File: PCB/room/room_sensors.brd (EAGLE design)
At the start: 90 x 90 mm, 112 parts, among them CON1 95278-101A14LF, CON2 95278-101A14LF, CON3 OV2640-HDF3M-811FRONTLOOKING, U1 BH1750FVI-TR, U12 LMR16020, U14 WM8974, U17 RT9043GB, U18 RT9043GB, U2 BME280, U3 CCS811B-JOPD500, U4 SN65HVD11DR, U5 SN65HVD11DR, U6 SN65HVD11DR, U7 SN65HVD11DR, U8 MAX14830ETMT, Y1 X1G004171001800 12MHz

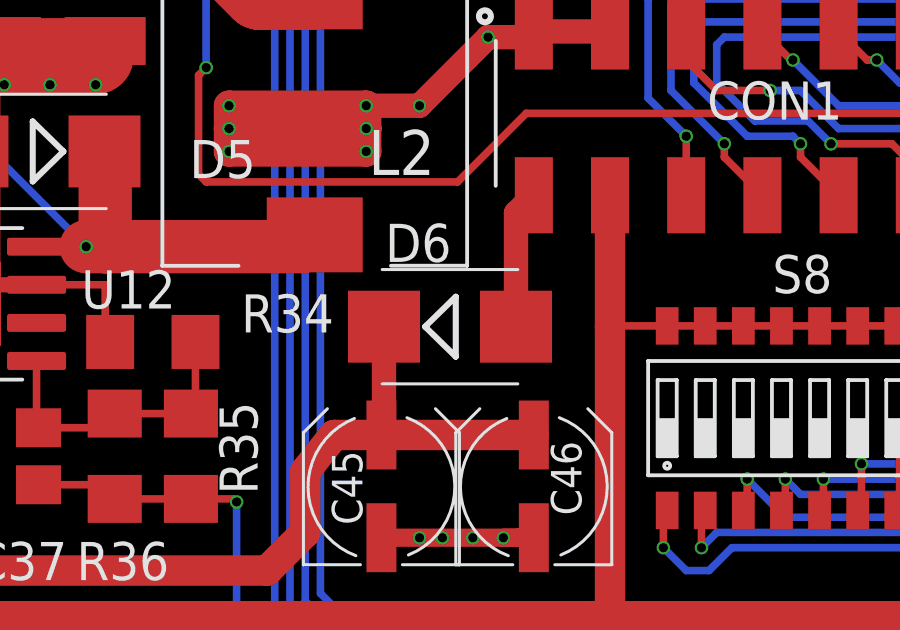
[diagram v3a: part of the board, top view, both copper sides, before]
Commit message: finished interface PCB
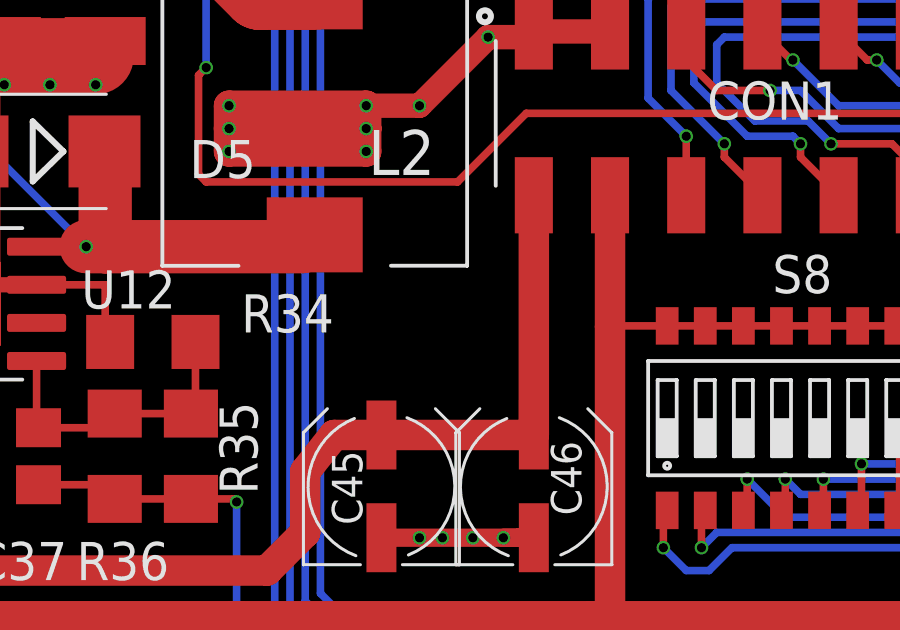
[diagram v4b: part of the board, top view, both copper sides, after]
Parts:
- removed D6: B360B-13-F, diode:SMB
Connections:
- removed net N$31: CON1.2, D6.A
- net +24V: now also CON1.2; no longer D6.C
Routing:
- net N$31: track 4.63 -> 0.00 mm
- net +24V: track 49.2 -> 53.6 mm
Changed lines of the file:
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@@
 <grid distance="10" unitdist="mil" unit="mil" style="lines" multiple="1" display="no" altdistance="1" altunitdist="mil" altunit="mil"/>
 <layers>
-<layer number="1" name="Top" color="4" fill="1" visible="no" active="yes"/>
+<layer number="1" name="Top" color="4" fill="1" visible="yes" active="yes"/>
 <layer number="2" name="Route2" color="1" fill="3" visible="no" active="no"/>
 <layer number="3" name="Route3" color="4" fill="3" visible="no" active="no"/>
@@
 <layer number="14" name="Route14" color="1" fill="6" visible="no" active="no"/>
 <layer number="15" name="Route15" color="4" fill="6" visible="no" active="no"/>
-<layer number="16" name="Bottom" color="1" fill="1" visible="yes" active="yes"/>
+<layer number="16" name="Bottom" color="1" fill="1" visible="no" active="yes"/>
 <layer number="17" name="Pads" color="2" fill="1" visible="no" active="yes"/>
 <layer number="18" name="Vias" color="2" fill="1" visible="no" active="yes"/>
-<layer number="19" name="Unrouted" color="6" fill="1" visible="no" active="yes"/>
+<layer number="19" name="Unrouted" color="6" fill="1" visible="yes" active="yes"/>
 <layer number="20" name="Dimension" color="15" fill="1" visible="no" active="yes"/>
 <layer number="21" name="tPlace" color="7" fill="1" visible="no" active="yes"/>
@@
 <attribute name="NAME" x="69.68003125" y="25.76643125" size="2.08761875" layer="25" ratio="10" rot="SR270"/>
 </element>
-<element name="D6" library="diode" package="SMB" value="B360B-13-F" x="35.306" y="17.018"/>
 </elements>
 <signals>
@@
 <wire x1="13.6525" y1="11.7475" x2="13.6525" y2="18.285" width="1.016" layer="1"/>
 <wire x1="13.6525" y1="18.285" x2="13.7825" y2="18.415" width="1.016" layer="1"/>
-<contactref element="D6" pad="C"/>
-<wire x1="33.106" y1="17.018" x2="33.106" y2="13.495" width="0.8128" layer="1"/>
 <wire x1="33.106" y1="13.495" x2="33.02" y2="13.409" width="0.8128" layer="1"/>
+<contactref element="CON1" pad="2"/>
+<wire x1="38.1" y1="21.4" x2="38.1" y2="13.409" width="1.016" layer="1"/>
 </signal>
 <signal name="N$32">
@@
 <wire x1="15.875" y1="20.385" x2="16.575" y2="19.685" width="0.254" layer="1"/>
 </signal>
-<signal name="N$31">
-<contactref element="CON1" pad="2"/>
-<contactref element="D6" pad="A"/>
-<wire x1="37.506" y1="17.018" x2="37.506" y2="20.806" width="0.8128" layer="1"/>
-<wire x1="37.506" y1="20.806" x2="38.1" y2="21.4" width="0.8128" layer="1"/>
-</signal>
 </signals>
-<errors>
-</errors>
 </board>
 </drawing>

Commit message: finished PCB designs
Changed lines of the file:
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@@
 <layer number="19" name="Unrouted" color="6" fill="1" visible="yes" active="yes"/>
 <layer number="20" name="Dimension" color="15" fill="1" visible="no" active="yes"/>
-<layer number="21" name="tPlace" color="7" fill="1" visible="no" active="yes"/>
+<layer number="21" name="tPlace" color="7" fill="1" visible="yes" active="yes"/>
 <layer number="22" name="bPlace" color="7" fill="1" visible="no" active="yes"/>
-<layer number="23" name="tOrigins" color="15" fill="1" visible="no" active="yes"/>
+<layer number="23" name="tOrigins" color="15" fill="1" visible="yes" active="yes"/>
 <layer number="24" name="bOrigins" color="15" fill="1" visible="no" active="yes"/>
-<layer number="25" name="tNames" color="7" fill="1" visible="no" active="yes"/>
+<layer number="25" name="tNames" color="7" fill="1" visible="yes" active="yes"/>
 <layer number="26" name="bNames" color="7" fill="1" visible="no" active="yes"/>
-<layer number="27" name="tValues" color="7" fill="1" visible="no" active="yes"/>
+<layer number="27" name="tValues" color="7" fill="1" visible="yes" active="yes"/>
 <layer number="28" name="bValues" color="7" fill="1" visible="no" active="yes"/>
-<layer number="29" name="tStop" color="7" fill="3" visible="no" active="yes"/>
+<layer number="29" name="tStop" color="7" fill="3" visible="yes" active="yes"/>
 <layer number="30" name="bStop" color="7" fill="6" visible="no" active="yes"/>
 <layer number="31" name="tCream" color="7" fill="4" visible="no" active="yes"/>
@@
 </element>
 <element name="R3" library="rcl" package="R1206" value="12k" x="54.864" y="51.181" smashed="yes" rot="R180">
-<attribute name="NAME" x="56.134" y="53.594" size="1.27" layer="25" rot="R180"/>
+<attribute name="NAME" x="55.88" y="49.784" size="1.27" layer="25" rot="R180"/>
 </element>
 <element name="C6" library="rcl" package="C0805" value="100nF 50V" x="40.64" y="53.34" smashed="yes">
@@
 </element>
 <element name="R7" library="rcl" package="R1206" value="100k" x="52.07" y="55.245" smashed="yes">
-<attribute name="NAME" x="54.2925" y="51.7525" size="1.27" layer="25" rot="R90"/>
+<attribute name="NAME" x="56.0705" y="54.2925" size="1.27" layer="25" rot="R90"/>
 </element>
 <element name="R9" library="rcl" package="R1206" value="4k7" x="31.75" y="42.164" smashed="yes" rot="R180">
@@
 </element>
 <element name="R19" library="rcl" package="R1206" value="120R" x="75.946" y="24.384" smashed="yes" rot="R270">
-<attribute name="NAME" x="77.089" y="23.749" size="1.27" layer="25"/>
+<attribute name="NAME" x="77.343" y="25.527" size="1.27" layer="25"/>
 </element>
 <element name="R20" library="rcl" package="R1206" value="1k" x="77.47" y="20.828" smashed="yes">
@@
 </element>
 <element name="R22" library="rcl" package="R1206" value="120R" x="74.422" y="36.068" smashed="yes">
-<attribute name="NAME" x="75.057" y="37.465" size="1.27" layer="25" rot="R90"/>
+<attribute name="NAME" x="76.073" y="42.037" size="1.27" layer="25" rot="R180"/>
 </element>
 <element name="R23" library="rcl" package="R1206" value="1k" x="77.978" y="37.592" smashed="yes" rot="R90">
@@
 </element>
 <element name="R25" library="rcl" package="R1206" value="120R" x="63.5" y="36.068" smashed="yes">
-<attribute name="NAME" x="64.135" y="37.338" size="1.27" layer="25" rot="R90"/>
+<attribute name="NAME" x="62.23" y="40.767" size="1.27" layer="25"/>
 </element>
 <element name="R26" library="rcl" package="R1206" value="1k" x="67.056" y="37.846" smashed="yes" rot="R90">
-<attribute name="NAME" x="65.786" y="36.576" size="1.27" layer="25" rot="R90"/>
+<attribute name="NAME" x="69.342" y="36.576" size="1.27" layer="25" rot="R90"/>
 </element>
 <element name="R27" library="rcl" package="R1206" value="1k" x="49.53" y="37.592" smashed="yes" rot="R270">
@@
 </element>
 <element name="R28" library="rcl" package="R1206" value="120R" x="53.086" y="36.068" smashed="yes">
-<attribute name="NAME" x="53.721" y="37.465" size="1.27" layer="25" rot="R90"/>
+<attribute name="NAME" x="54.483" y="42.037" size="1.27" layer="25" rot="R180"/>
 </element>
 <element name="R29" library="rcl" package="R1206" value="1k" x="56.642" y="37.592" smashed="yes" rot="R90">
@@
 </element>
 <element name="R30" library="rcl" package="R1206" value="4k7" x="19.304" y="42.164" smashed="yes" rot="R180">
-<attribute name="NAME" x="20.8915" y="44.704" size="1.27" layer="25" rot="R180"/>
+<attribute name="NAME" x="20.6375" y="40.894" size="1.27" layer="25" rot="R180"/>
 </element>
 <element name="C31" library="rcl" package="C0805" value="4u7 16V" x="45.72" y="34.29" smashed="yes" rot="R90">
@@
 <attribute name="DESCRIPTION" value=" RS-485 Interface ICs 3.3V Differential Transceivers " x="53.34" y="32.004" size="1.778" layer="27" display="off"/>
 <attribute name="MF" value="Texas Instruments" x="53.34" y="32.004" size="1.778" layer="27" display="off"/>
-<attribute name="NAME" x="51.44956875" y="29.80203125" size="2.08761875" layer="25" ratio="10" rot="SR0"/>
+<attribute name="NAME" x="52.46556875" y="31.32603125" size="1.27" layer="25" ratio="10" rot="SR0"/>
 </element>
 <element name="U5" library="SN65HVD11DR_snapEDA" package="SOIC127P600X175-8N" value="SN65HVD11DR" x="63.5" y="32.004" smashed="yes">
@@
 <attribute name="DESCRIPTION" value=" RS-485 Interface ICs 3.3V Differential Transceivers " x="63.5" y="32.004" size="1.778" layer="27" display="off"/>
 <attribute name="MF" value="Texas Instruments" x="63.5" y="32.004" size="1.778" layer="27" display="off"/>
-<attribute name="NAME" x="61.60956875" y="29.54803125" size="2.08761875" layer="25" ratio="10" rot="SR0"/>
+<attribute name="NAME" x="62.37156875" y="31.32603125" size="1.27" layer="25" ratio="10" rot="SR0"/>
 </element>
 <element name="U6" library="SN65HVD11DR_snapEDA" package="SOIC127P600X175-8N" value="SN65HVD11DR" x="73.66" y="32.004" smashed="yes">
@@
 <attribute name="DESCRIPTION" value=" RS-485 Interface ICs 3.3V Differential Transceivers " x="73.66" y="32.004" size="1.778" layer="27" display="off"/>
 <attribute name="MF" value="Texas Instruments" x="73.66" y="32.004" size="1.778" layer="27" display="off"/>
-<attribute name="NAME" x="71.76956875" y="29.80203125" size="2.08761875" layer="25" ratio="10" rot="SR0"/>
+<attribute name="NAME" x="72.53156875" y="31.32603125" size="1.27" layer="25" ratio="10" rot="SR0"/>
 </element>
 <element name="U7" library="SN65HVD11DR_snapEDA" package="SOIC127P600X175-8N" value="SN65HVD11DR" x="71.882" y="24.13" smashed="yes" rot="R270">
@@
 <attribute name="DESCRIPTION" value=" RS-485 Interface ICs 3.3V Differential Transceivers " x="71.882" y="24.13" size="1.778" layer="27" rot="R270" display="off"/>
 <attribute name="MF" value="Texas Instruments" x="71.882" y="24.13" size="1.778" layer="27" rot="R270" display="off"/>
-<attribute name="NAME" x="69.68003125" y="25.76643125" size="2.08761875" layer="25" ratio="10" rot="SR270"/>
+<attribute name="NAME" x="70.95003125" y="25.25843125" size="1.27" layer="25" ratio="10" rot="SR270"/>
 </element>
 </elements>
